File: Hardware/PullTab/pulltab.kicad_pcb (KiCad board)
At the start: 2 copper layers, 22.1 x 21.3 mm, 9 parts, among them J1 Switch_Junction, J2 GND_IN, J4 VBAT_IN, J5 Switch_NC, J6 VBAT_OUT, J7 GND_OUT, Q1 NMOS

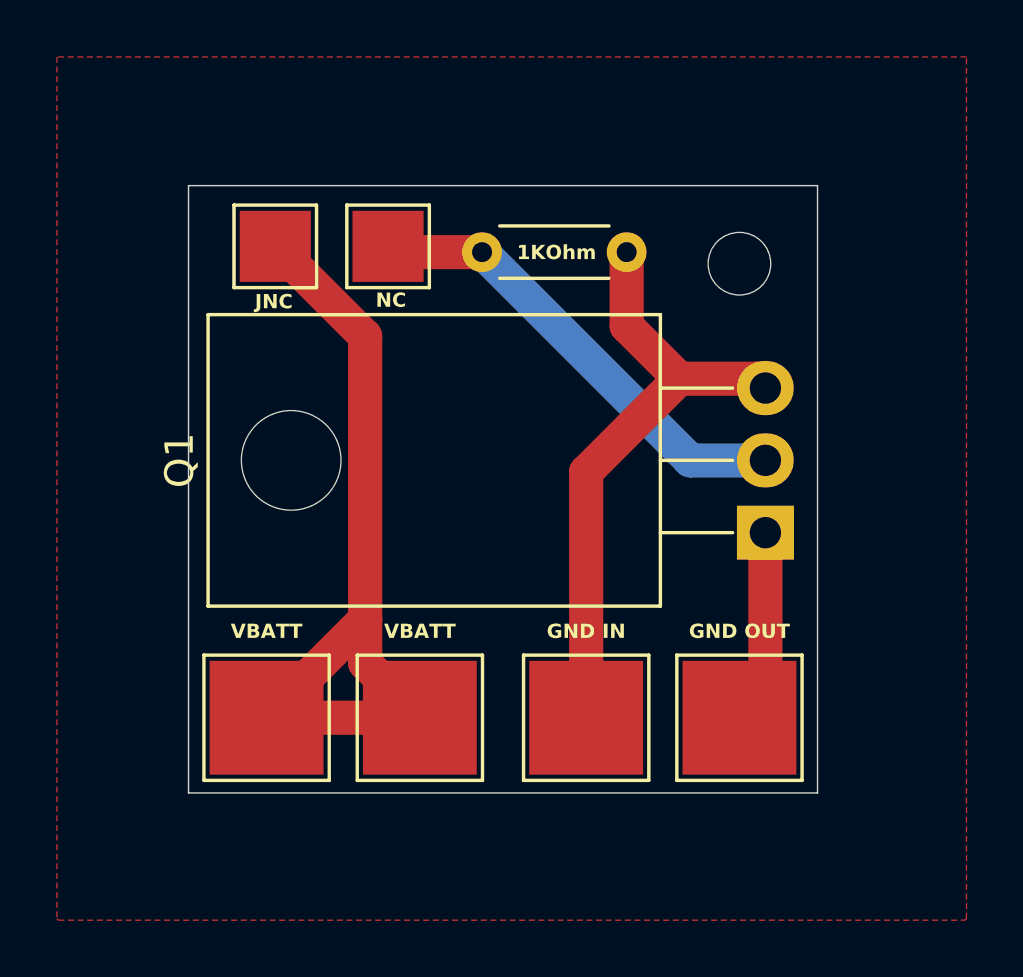
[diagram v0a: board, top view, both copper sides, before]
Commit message: fixed pulltab mosfet pin orientation added cad
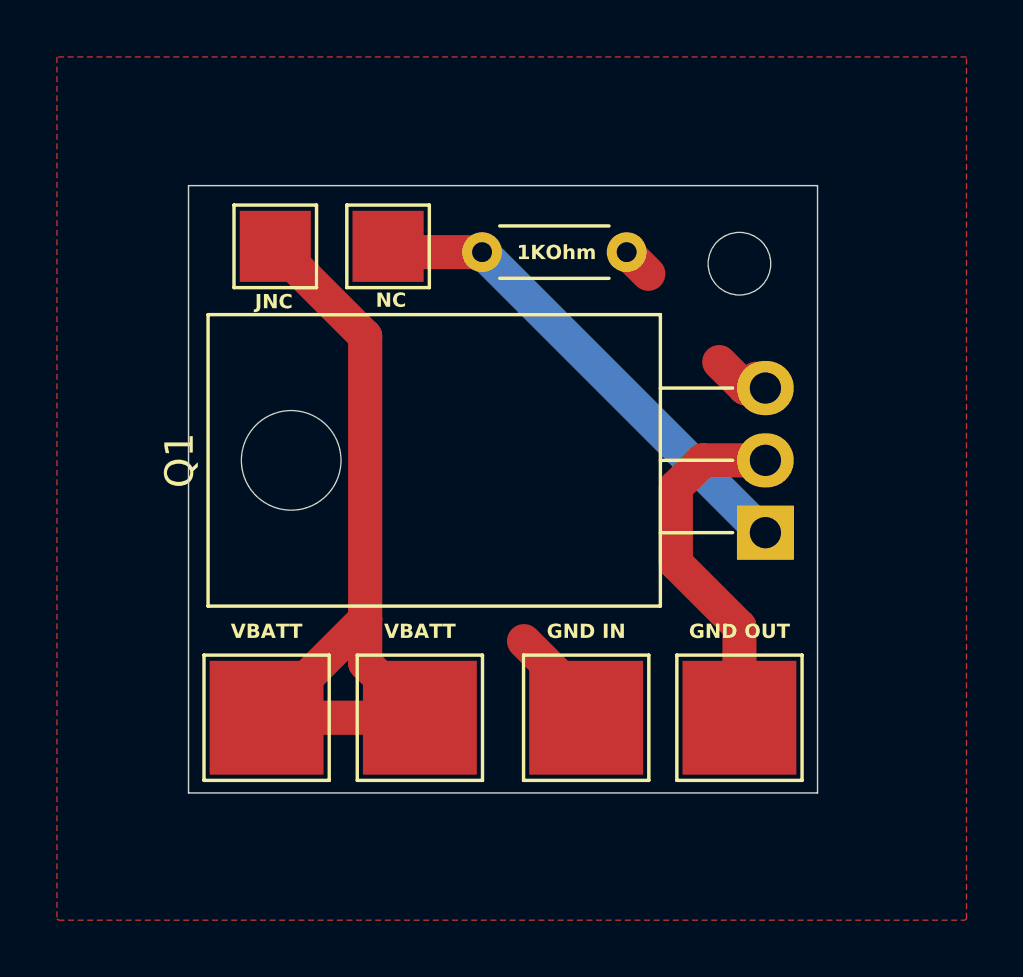
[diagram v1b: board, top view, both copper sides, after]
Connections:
- Q1 pad 1: Net-(J7-Pin_1) -> Net-(J1-Pin_1)
- Q1 pad 2: Net-(J1-Pin_1) -> Net-(J7-Pin_1)
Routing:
- net GND: track 21.6 -> 7.14 mm
- net Net-(J7-Pin_1): track 6.88 -> 13.9 mm
- net Net-(J1-Pin_1): track 16.4 -> 17.4 mm
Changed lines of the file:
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@@
 			(layers "*.Cu" "*.Mask")
 			(remove_unused_layers no)
-			(net 4 "Net-(J7-Pin_1)")
-			(pinfunction "D")
-			(pintype "passive")
+			(net 1 "Net-(J1-Pin_1)")
+			(pinfunction "G")
+			(pintype "input")
 		)
 		(pad "2" thru_hole oval
@@
 			(layers "*.Cu" "*.Mask")
 			(remove_unused_layers no)
-			(net 1 "Net-(J1-Pin_1)")
-			(pinfunction "G")
-			(pintype "input")
+			(net 4 "Net-(J7-Pin_1)")
+			(pinfunction "D")
+			(pintype "passive")
 		)
 		(pad "3" thru_hole oval
@@
 		(tags "Resistor Axial_DIN0204 series Axial Horizontal pin pitch 5.08mm 0.167W length 3.6mm diameter 1.6mm")
 		(property "Reference" "R1"
-			(at 2.54 -1.92 360)
+			(at 2.54 -1.92 0)
 			(layer "F.SilkS")
 			(hide yes)
@@
 		)
 		(property "Value" "1k"
-			(at 2.54 1.92 360)
+			(at 2.54 1.92 0)
 			(layer "F.Fab")
 			(effects
@@
 		)
 		(fp_text user "${REFERENCE}"
-			(at 2.54 0 360)
+			(at 2.54 0 0)
 			(layer "F.Fab")
 			(effects
@@
 	)
 	(segment
-		(start 142.0344 69.4436)
-		(end 139.3952 69.4436)
+		(start 141.9352 71.9836)
+		(end 132.08 62.1284)
 		(width 1.2)
 		(layer "B.Cu")
@@
 	)
 	(segment
-		(start 139.3952 69.4436)
-		(end 132.08 62.1284)
+		(start 142.0344 71.9836)
+		(end 141.9352 71.9836)
 		(width 1.2)
 		(layer "B.Cu")
@@
 	)
 	(segment
-		(start 141.7054 66.5746)
-		(end 139.013 66.5746)
-		(width 1.2)
-		(layer "F.Cu")
-		(net 2)
-	)
-	(segment
-		(start 137.159999 62.1284)
-		(end 137.159999 64.721599)
-		(width 1.2)
-		(layer "F.Cu")
-		(net 2)
-	)
-	(segment
-		(start 137.159999 64.721599)
-		(end 139.013 66.5746)
+		(start 142.0344 66.903601)
+		(end 141.325601 66.903601)
 		(width 1.2)
 		(layer "F.Cu")
@@
 	)
 	(segment
-		(start 135.7376 69.85)
-		(end 135.7376 78.486)
+		(start 135.7376 77.978)
+		(end 133.5532 75.7936)
 		(width 1.2)
 		(layer "F.Cu")
@@
 	)
 	(segment
-		(start 139.013 66.5746)
-		(end 135.7376 69.85)
+		(start 137.159999 62.1284)
+		(end 137.922 62.890401)
+		(width 1.2)
+		(layer "F.Cu")
+		(net 2)
+	)
+	(segment
+		(start 141.325601 66.903601)
+		(end 140.4112 65.9892)
+		(width 1.2)
+		(layer "F.Cu")
+		(net 2)
+	)
+	(segment
+		(start 135.7376 78.486)
+		(end 135.7376 77.978)
 		(width 1.2)
 		(layer "F.Cu")
@@
 	)
 	(segment
+		(start 139.8344 69.4436)
+		(end 142.0344 69.4436)
+		(width 1.2)
+		(layer "F.Cu")
+		(net 4)
+	)
+	(segment
+		(start 141.1224 78.486)
+		(end 141.1224 75.2856)
+		(width 1.2)
+		(layer "F.Cu")
+		(net 4)
+	)
+	(segment
 		(start 142.0344 77.574)
 		(end 141.1224 78.486)
@@
 	)
 	(segment
-		(start 142.0344 71.9836)
-		(end 142.0344 77.574)
-		(width 1.2)
-		(layer "F.Cu")
+		(start 138.8872 70.3908)
+		(end 139.8344 69.4436)
+		(width 1.2)
+		(layer "F.Cu")
+		(net 4)
+	)
+	(segment
+		(start 141.1224 75.2856)
+		(end 138.8872 73.0504)
+		(width 1.2)
+		(layer "F.Cu")
+		(net 4)
+	)
+	(segment
+		(start 138.8872 73.0504)
+		(end 138.8872 70.3908)
+		(width 1.2)
+		(layer "F.Cu")
